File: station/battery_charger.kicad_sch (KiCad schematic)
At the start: 1 part, among them J8 Conn_01x04

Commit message: Signed-off-by: Scott Perkins <whatisbyandby@gmail.com>
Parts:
- removed J8: Conn_01x04, Connector_PinSocket_2.54mm:PinSocket_1x04_P2.54mm_Horizontal, symbol Connector_Generic:Conn_01x04
- added J8: Battery Charger, Connector_PinSocket_2.54mm:PinSocket_2x03_P2.54mm_Vertical, symbol Connector_Generic:Conn_02x03_Counter_Clockwise
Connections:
- net SET: now also J8.4 (Pin_4)
- net ~{CHRG}: now also J8.6 (Pin_6)
- net ~{FAULT}: now also J8.5 (Pin_5)
- new net GND: J8.2 (Pin_2), J8.3 (Pin_3)
- new net Load+: J8.1 (Pin_1)
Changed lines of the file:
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@@
 	(generator_version "8.0")
 	(paper "A4")
-	(wire
-		(pts
-			(xy 109.22 91.44) (xy 115.57 91.44)
-		)
-		(stroke
-			(width 0)
-			(type default)
-		)
-	)
-	(wire
-		(pts
-			(xy 109.22 86.36) (xy 115.57 86.36)
-		)
-		(stroke
-			(width 0)
-			(type default)
-		)
-	)
-	(wire
-		(pts
-			(xy 109.22 88.9) (xy 115.57 88.9)
-		)
-		(stroke
-			(width 0)
-			(type default)
-		)
-	)
-	(wire
-		(pts
-			(xy 109.22 93.98) (xy 115.57 93.98)
+	(junction
+		(at 113.03 87.63)
+		(diameter 0)
+		(color 0 0 0 0)
+	)
+	(junction
+		(at 113.03 85.09)
+		(diameter 0)
+		(color 0 0 0 0)
+	)
+	(wire
+		(pts
+			(xy 125.73 87.63) (xy 130.81 87.63)
+		)
+		(stroke
+			(width 0)
+			(type default)
+		)
+	)
+	(wire
+		(pts
+			(xy 113.03 87.63) (xy 113.03 90.17)
+		)
+		(stroke
+			(width 0)
+			(type default)
+		)
+	)
+	(wire
+		(pts
+			(xy 111.76 85.09) (xy 113.03 85.09)
+		)
+		(stroke
+			(width 0)
+			(type default)
+		)
+	)
+	(wire
+		(pts
+			(xy 125.73 82.55) (xy 130.81 82.55)
+		)
+		(stroke
+			(width 0)
+			(type default)
+		)
+	)
+	(wire
+		(pts
+			(xy 125.73 85.09) (xy 130.81 85.09)
+		)
+		(stroke
+			(width 0)
+			(type default)
+		)
+	)
+	(wire
+		(pts
+			(xy 113.03 85.09) (xy 113.03 87.63)
+		)
+		(stroke
+			(width 0)
+			(type default)
+		)
+	)
+	(wire
+		(pts
+			(xy 111.76 82.55) (xy 113.03 82.55)
 		)
 		(stroke
@@
 	(hierarchical_label "~{CHRG}"
 		(shape output)
-		(at 115.57 86.36 0)
+		(at 130.81 82.55 0)
 		(fields_autoplaced yes)
 		(effects
@@
 	(hierarchical_label "~{FAULT}"
 		(shape output)
-		(at 115.57 88.9 0)
+		(at 130.81 85.09 0)
 		(fields_autoplaced yes)
 		(effects
@@
 	(hierarchical_label "SET"
 		(shape input)
-		(at 115.57 91.44 0)
+		(at 130.81 87.63 0)
 		(fields_autoplaced yes)
 		(effects
@@
 		)
 	)
-	(hierarchical_label "VOUT"
-		(shape output)
-		(at 115.57 93.98 0)
-		(fields_autoplaced yes)
-		(effects
-			(font
-				(size 1.27 1.27)
-			)
-			(justify left)
+	(hierarchical_label "Load+"
+		(shape passive)
+		(at 111.76 82.55 180)
+		(fields_autoplaced yes)
+		(effects
+			(font
+				(size 1.27 1.27)
+			)
+			(justify right)
+		)
+	)
+	(hierarchical_label "Load-"
+		(shape passive)
+		(at 111.76 85.09 180)
+		(fields_autoplaced yes)
+		(effects
+			(font
+				(size 1.27 1.27)
+			)
+			(justify right)
 		)
 	)
 	(symbol
-		(lib_id "Connector_Generic:Conn_01x04")
-		(at 104.14 91.44 180)
+		(lib_id "power:GND")
+		(at 113.03 90.17 0)
 		(unit 1)
 		(exclude_from_sim no)
@@
 		(dnp no)
 		(fields_autoplaced yes)
+		(property "Reference" "#PWR024"
+			(at 113.03 96.52 0)
+			(effects
+				(font
+					(size 1.27 1.27)
+				)
+				(hide yes)
+			)
+		)
+		(property "Value" "GND"
+			(at 113.03 95.25 0)
+			(effects
+				(font
+					(size 1.27 1.27)
+				)
+			)
+		)
+		(property "Footprint" ""
+			(at 113.03 90.17 0)
+			(effects
+				(font
+					(size 1.27 1.27)
+				)
+				(hide yes)
+			)
+		)
+		(property "Datasheet" ""
+			(at 113.03 90.17 0)
+			(effects
+				(font
+					(size 1.27 1.27)
+				)
+				(hide yes)
+			)
+		)
+		(property "Description" "Power symbol creates a global label with name \"GND\" , ground"
+			(at 113.03 90.17 0)
+			(effects
+				(font
+					(size 1.27 1.27)
+				)
+				(hide yes)
+			)
+		)
+		(pin "1"
+		)
+		(instances
+			(project "weather_station_pico"
+				(path "/8f1f45aa-e764-4c95-a223-c466cf9a95bf/42d4f7d6-4f97-4f29-a0cd-bf4a015f7c0a"
+					(reference "#PWR024")
+					(unit 1)
+				)
+			)
+		)
+	)
+	(symbol
+		(lib_id "Connector_Generic:Conn_02x03_Counter_Clockwise")
+		(at 118.11 85.09 0)
+		(unit 1)
+		(exclude_from_sim no)
+		(in_bom yes)
+		(on_board yes)
+		(dnp no)
+		(fields_autoplaced yes)
 		(property "Reference" "J8"
-			(at 104.14 80.01 0)
-			(effects
-				(font
-					(size 1.27 1.27)
-				)
-			)
-		)
-		(property "Value" "Conn_01x04"
-			(at 104.14 82.55 0)
-			(effects
-				(font
-					(size 1.27 1.27)
-				)
-			)
-		)
-		(property "Footprint" "Connector_PinSocket_2.54mm:PinSocket_1x04_P2.54mm_Horizontal"
-			(at 104.14 91.44 0)
+			(at 119.38 76.2 0)
+			(effects
+				(font
+					(size 1.27 1.27)
+				)
+			)
+		)
+		(property "Value" "Battery Charger"
+			(at 119.38 78.74 0)
+			(effects
+				(font
+					(size 1.27 1.27)
+				)
+			)
+		)
+		(property "Footprint" "Connector_PinSocket_2.54mm:PinSocket_2x03_P2.54mm_Vertical"
+			(at 118.11 85.09 0)
 			(effects
 				(font
@@
 		)
 		(property "Datasheet" "~"
-			(at 104.14 91.44 0)
-			(effects
-				(font
-					(size 1.27 1.27)
-				)
-				(hide yes)
-			)
-		)
-		(property "Description" "Generic connector, single row, 01x04, script generated (kicad-library-utils/schlib/autogen/connector/)"
-			(at 104.14 91.44 0)
-			(effects
-				(font
-					(size 1.27 1.27)
-				)
-				(hide yes)
-			)
+			(at 118.11 85.09 0)
+			(effects
+				(font
+					(size 1.27 1.27)
+				)
+				(hide yes)
+			)
+		)
+		(property "Description" "Generic connector, double row, 02x03, counter clockwise pin numbering scheme (similar to DIP package numbering), script generated (kicad-library-utils/schlib/autogen/connector/)"
+			(at 118.11 85.09 0)
+			(effects
+				(font
+					(size 1.27 1.27)
+				)
+				(hide yes)
+			)
+		)
+		(pin "2"
+		)
+		(pin "5"
+		)
+		(pin "6"
+		)
+		(pin "1"
 		)
 		(pin "3"
 		)
-		(pin "2"
-		)
 		(pin "4"
 		)
-		(pin "1"
-		)
 		(instances

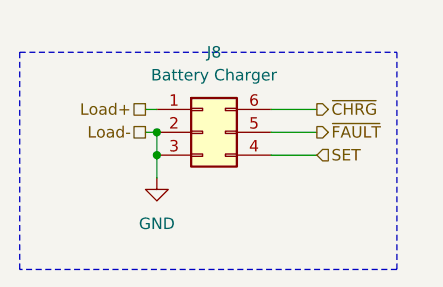
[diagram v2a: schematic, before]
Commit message: Switched to a round board
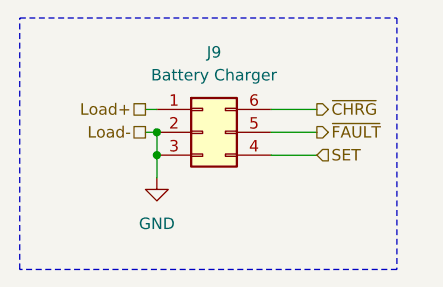
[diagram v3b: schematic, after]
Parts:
- renumbered J8 to J9
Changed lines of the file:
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@@
 	)
 	(rectangle
-		(start 97.79 76.2)
+		(start 97.79 72.39)
 		(end 139.7 100.33)
 		(stroke
@@
 		(dnp no)
 		(fields_autoplaced yes)
-		(property "Reference" "#PWR030"
+		(property "Reference" "#PWR033"
 			(at 113.03 96.52 0)
 			(effects
@@
 			(project "weather_station_pico"
 				(path "/8f1f45aa-e764-4c95-a223-c466cf9a95bf/42d4f7d6-4f97-4f29-a0cd-bf4a015f7c0a"
-					(reference "#PWR030")
+					(reference "#PWR033")
 					(unit 1)
 				)
@@
 		(dnp no)
 		(fields_autoplaced yes)
-		(property "Reference" "J8"
+		(property "Reference" "J9"
 			(at 119.38 76.2 0)
 			(effects
@@
 			(project "weather_station_pico"
 				(path "/8f1f45aa-e764-4c95-a223-c466cf9a95bf/42d4f7d6-4f97-4f29-a0cd-bf4a015f7c0a"
-					(reference "J8")
+					(reference "J9")
 					(unit 1)
 				)

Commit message: Added a reset button, status LEDs and broke out UART pins
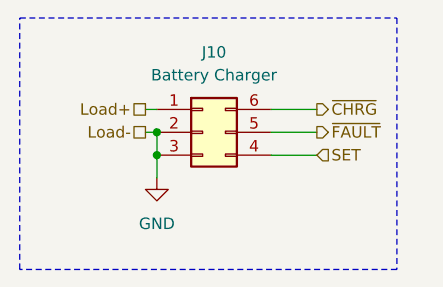
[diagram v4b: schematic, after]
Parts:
- renumbered J9 to J10
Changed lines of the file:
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@@
 		(dnp no)
 		(fields_autoplaced yes)
-		(property "Reference" "#PWR033"
+		(property "Reference" "#PWR037"
 			(at 113.03 96.52 0)
 			(effects
@@
 			(project "weather_station_pico"
 				(path "/8f1f45aa-e764-4c95-a223-c466cf9a95bf/42d4f7d6-4f97-4f29-a0cd-bf4a015f7c0a"
-					(reference "#PWR033")
+					(reference "#PWR037")
 					(unit 1)
 				)
@@
 		(dnp no)
 		(fields_autoplaced yes)
-		(property "Reference" "J9"
+		(property "Reference" "J10"
 			(at 119.38 76.2 0)
 			(effects
@@
 			(project "weather_station_pico"
 				(path "/8f1f45aa-e764-4c95-a223-c466cf9a95bf/42d4f7d6-4f97-4f29-a0cd-bf4a015f7c0a"
-					(reference "J9")
+					(reference "J10")
 					(unit 1)
 				)
